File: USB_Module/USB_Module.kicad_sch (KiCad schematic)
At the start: 4 parts, among them J1 USB_A, J3 Conn_01x02_Pin, J4 Conn_01x08_Socket, J5 Conn_01x10_Socket

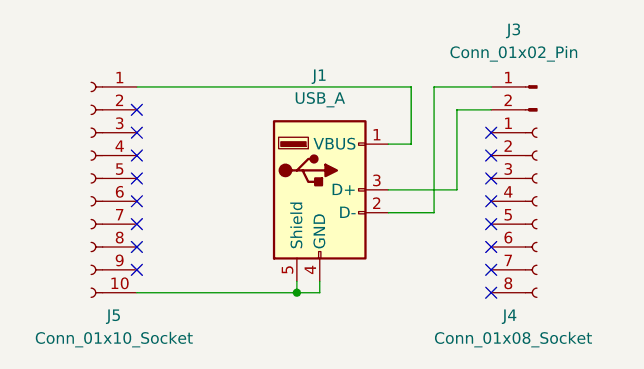
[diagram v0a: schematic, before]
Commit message: Updating USB PCB desing
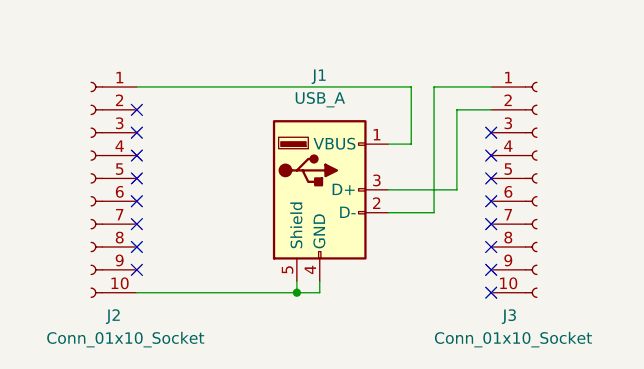
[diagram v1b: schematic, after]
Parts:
- removed J3: Conn_01x02_Pin, Connector_PinHeader_2.00mm:PinHeader_1x02_P2.00mm_Vertical, symbol Connector:Conn_01x02_Pin
- removed J4: Conn_01x08_Socket, Connector_PinSocket_2.00mm:PinSocket_1x08_P2.00mm_Vertical, symbol Connector:Conn_01x08_Socket
- added J3: Conn_01x10_Socket, Connector_PinSocket_2.00mm:PinSocket_1x10_P2.00mm_Vertical, symbol Connector:Conn_01x10_Socket
- renumbered J5 to J2
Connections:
- net at J1.2 (D-): now also J3.1 (Pin_1)
- net at J1.3 (D+): now also J3.2 (Pin_2)
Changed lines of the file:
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@@
   (junction (at 119.38 99.06) (diameter 0) (color 0 0 0 0)
   )
+  (no_connect (at 140.97 86.36))
   (no_connect (at 101.6 86.36))
-  (no_connect (at 140.97 86.36))
-  (no_connect (at 140.97 83.82))
   (no_connect (at 101.6 91.44))
+  (no_connect (at 140.97 88.9))
   (no_connect (at 101.6 81.28))
   (no_connect (at 101.6 88.9))
   (no_connect (at 101.6 93.98))
   (no_connect (at 101.6 83.82))
+  (no_connect (at 101.6 96.52))
+  (no_connect (at 140.97 93.98))
   (no_connect (at 140.97 81.28))
-  (no_connect (at 101.6 96.52))
-  (no_connect (at 140.97 91.44))
-  (no_connect (at 140.97 93.98))
+  (no_connect (at 140.97 83.82))
   (no_connect (at 101.6 78.74))
   (no_connect (at 140.97 96.52))
-  (no_connect (at 140.97 88.9))
+  (no_connect (at 140.97 91.44))
   (no_connect (at 140.97 99.06))
-  (wire (pts (xy 134.62 76.2) (xy 140.97 76.2))
-    (stroke (width 0) (type default))
-  )
   (wire (pts (xy 129.54 87.63) (xy 137.16 87.63))
     (stroke (width 0) (type default))
@@
   )
   (wire (pts (xy 137.16 78.74) (xy 140.97 78.74))
+    (stroke (width 0) (type default))
+  )
+  (wire (pts (xy 134.62 76.2) (xy 140.97 76.2))
     (stroke (width 0) (type default))
   )
@@
     )
   )
-  (symbol (lib_id "Connector:Conn_01x02_Pin") (at 146.05 76.2 0) (mirror y) (unit 1)
+  (symbol (lib_id "Connector:Conn_01x10_Socket") (at 146.05 86.36 0) (unit 1)
     (in_bom yes) (on_board yes) (dnp no)
-    (property "Reference" "J3" (at 143.51 69.85 0)
-      (effects (font (size 1.27 1.27)))
+    (property "Reference" "J3" (at 142.24 101.6 0)
+      (effects (font (size 1.27 1.27)) (justify left))
     )
-    (property "Value" "Conn_01x02_Pin" (at 143.51 72.39 0)
-      (effects (font (size 1.27 1.27)))
+    (property "Value" "Conn_01x10_Socket" (at 134.62 104.14 0)
+      (effects (font (size 1.27 1.27)) (justify left))
     )
-    (property "Footprint" "Connector_PinHeader_2.00mm:PinHeader_1x02_P2.00mm_Vertical" (at 146.05 76.2 0)
+    (property "Footprint" "Connector_PinSocket_2.00mm:PinSocket_1x10_P2.00mm_Vertical" (at 146.05 86.36 0)
       (effects (font (size 1.27 1.27)) hide)
     )
-    (property "Datasheet" "~" (at 146.05 76.2 0)
+    (property "Datasheet" "~" (at 146.05 86.36 0)
       (effects (font (size 1.27 1.27)) hide)
     )
     (pin "1")
+    (pin "10")
     (pin "2")
+    (pin "3")
+    (pin "4")
+    (pin "5")
+    (pin "6")
+    (pin "7")
+    (pin "8")
+    (pin "9")
     (instances
       (project "USB_Module"
@@
     )
   )
-  (symbol (lib_id "Connector:Conn_01x08_Socket") (at 146.05 88.9 0) (unit 1)
-    (in_bom yes) (on_board yes) (dnp no)
-    (property "Reference" "J4" (at 142.24 101.6 0)
-      (effects (font (size 1.27 1.27)) (justify left))
-    )
-    (property "Value" "Conn_01x08_Socket" (at 134.62 104.14 0)
-      (effects (font (size 1.27 1.27)) (justify left))
-    )
-    (property "Footprint" "Connector_PinSocket_2.00mm:PinSocket_1x08_P2.00mm_Vertical" (at 146.05 88.9 0)
-      (effects (font (size 1.27 1.27)) hide)
-    )
-    (property "Datasheet" "~" (at 146.05 88.9 0)
-      (effects (font (size 1.27 1.27)) hide)
-    )
-    (pin "1")
-    (pin "2")
-    (pin "3")
-    (pin "4")
-    (pin "5")
-    (pin "6")
-    (pin "7")
-    (pin "8")
-    (instances
-      (project "USB_Module"
-        (path "/d452682e-4b72-4fc8-ac9a-c22d1abda260"
-          (reference "J4") (unit 1)
-        )
-      )
-    )
-  )
   (symbol (lib_id "Connector:Conn_01x10_Socket") (at 96.52 86.36 0) (mirror y) (unit 1)
     (in_bom yes) (on_board yes) (dnp no)
-    (property "Reference" "J5" (at 99.06 101.6 0)
+    (property "Reference" "J2" (at 99.06 101.6 0)
       (effects (font (size 1.27 1.27)))
     )
-    (property "Value" "Conn_01x10_Socket" (at 99.06 104.14 0)
+    (property "Value" "Conn_01x10_Socket" (at 100.33 104.14 0)
       (effects (font (size 1.27 1.27)))
     )
@@
       (project "USB_Module"
         (path "/d452682e-4b72-4fc8-ac9a-c22d1abda260"
-          (reference "J5") (unit 1)
+          (reference "J2") (unit 1)
         )
       )

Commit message: Adding first version of GigE PCB design
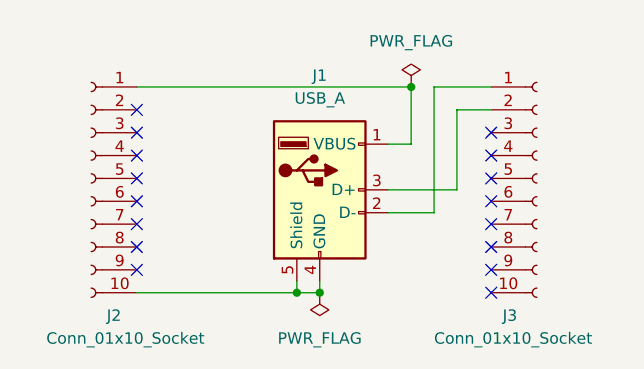
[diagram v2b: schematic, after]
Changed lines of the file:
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@@
 (kicad_sch (version 20230121) (generator eeschema)
   (paper "A4")
+  (junction (at 121.92 99.06) (diameter 0) (color 0 0 0 0)
+  )
   (junction (at 119.38 99.06) (diameter 0) (color 0 0 0 0)
+  )
+  (junction (at 132.08 76.2) (diameter 0) (color 0 0 0 0)
   )
   (no_connect (at 140.97 86.36))
@@
         )
       )
+    )
+  )
+  (symbol (lib_id "power:PWR_FLAG") (at 132.08 76.2 0) (unit 1)
+    (in_bom yes) (on_board yes) (dnp no) (fields_autoplaced)
+    (property "Reference" "#FLG02" (at 132.08 74.295 0)
+      (effects (font (size 1.27 1.27)) hide)
+    )
+    (property "Value" "PWR_FLAG" (at 132.08 71.12 0)
+      (effects (font (size 1.27 1.27)))
+    )
+    (property "Footprint" "" (at 132.08 76.2 0)
+      (effects (font (size 1.27 1.27)) hide)
+    )
+    (property "Datasheet" "~" (at 132.08 76.2 0)
+      (effects (font (size 1.27 1.27)) hide)
+    )
+    (pin "1")
+    (instances
+      (project "USB_Module"
+        (path "/d452682e-4b72-4fc8-ac9a-c22d1abda260"
+          (reference "#FLG02") (unit 1)
+        )
+      )
+    )
+  )
+  (symbol (lib_id "power:PWR_FLAG") (at 121.92 99.06 180) (unit 1)
+    (in_bom yes) (on_board yes) (dnp no) (fields_autoplaced)
+    (property "Reference" "#FLG01" (at 121.92 100.965 0)
+      (effects (font (size 1.27 1.27)) hide)
+    )
+    (property "Value" "PWR_FLAG" (at 121.92 104.14 0)
+      (effects (font (size 1.27 1.27)))
+    )
+    (property "Footprint" "" (at 121.92 99.06 0)
+      (effects (font (size 1.27 1.27)) hide)
+    )
+    (property "Datasheet" "~" (at 121.92 99.06 0)
+      (effects (font (size 1.27 1.27)) hide)
+    )
+    (pin "1")
+    (instances
+      (project "USB_Module"
+        (path "/d452682e-4b72-4fc8-ac9a-c22d1abda260"
+          (reference "#FLG01") (unit 1)
+        )
+      )
